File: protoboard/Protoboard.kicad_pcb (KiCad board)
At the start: 2 copper layers, 99.8 x 99.8 mm, 91 parts, among them J1 Conn_02x32_Odd_Even, J2 Conn_02x32_Odd_Even

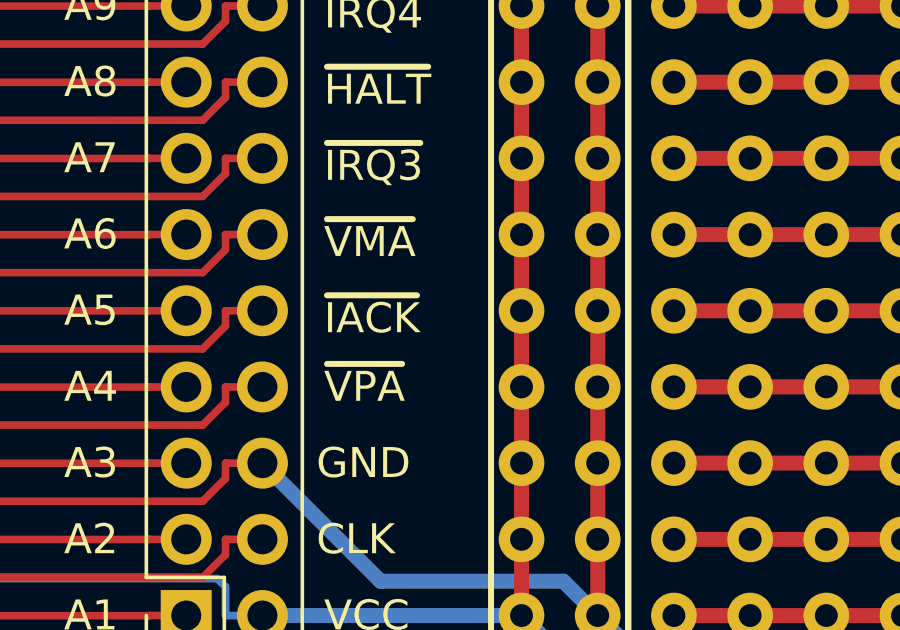
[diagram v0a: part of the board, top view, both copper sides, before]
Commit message: Added a status output board
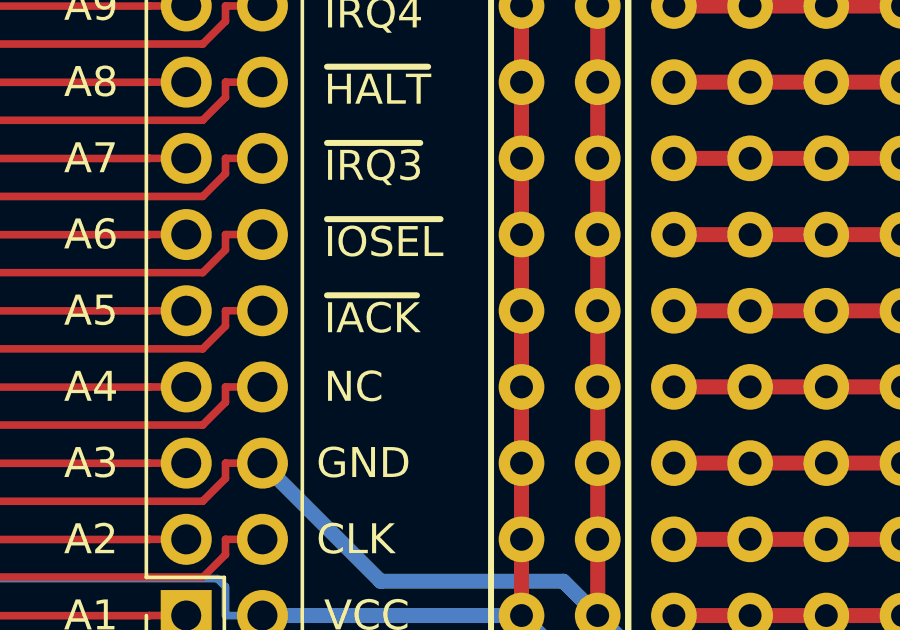
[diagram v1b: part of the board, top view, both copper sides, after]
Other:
- board text added: "NC"
- board text added: "~{IOSEL}"
- board text removed: "~{VMA}"
- board text removed: "~{VPA}"
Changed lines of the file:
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@@
     (effects (font (size 1 1) (thickness 0.2)) (justify right))
   )
-  (gr_text "~{VPA}" (at 117.114 128.27) (layer "F.SilkS")
+  (gr_text "NC" (at 117.114 128.27) (layer "F.SilkS")
     (effects (font (size 1 1) (thickness 0.2)) (justify left))
   )
@@
     (effects (font (size 3 3) (thickness 0.3)))
   )
-  (gr_text "~{VMA}" (at 117.114 123.444) (layer "F.SilkS")
+  (gr_text "~{IOSEL}" (at 117.114 123.444) (layer "F.SilkS")
     (effects (font (size 1 1) (thickness 0.2)) (justify left))
   )

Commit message: checkpoint
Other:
- board text added: "VPA"
- board text removed: "NC"
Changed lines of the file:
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@@
     (effects (font (size 1 1) (thickness 0.2)) (justify right))
   )
-  (gr_text "NC" (at 117.114 128.27) (layer "F.SilkS")
+  (gr_text "VPA" (at 117.114 128.27) (layer "F.SilkS")
     (effects (font (size 1 1) (thickness 0.2)) (justify left))
   )
